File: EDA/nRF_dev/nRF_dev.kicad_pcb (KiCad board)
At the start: 2 copper layers, 52 x 82.7 mm, 60 parts, among them J1 USB_B_Micro, J2 Conn_01x02, J3 Conn_02x18_Odd_Even, J4 Conn_02x18_Odd_Even, J5 OV7675_DBG, J6 FH26W-25S-0.3SHW(60), J7 SWD, U1 NCP1117-3.3_SOT223, U2 W25Q128JVS, U3 RP2040, U4 OV7675pcb, Y1 ABLS-12.000MHZ-B4-T

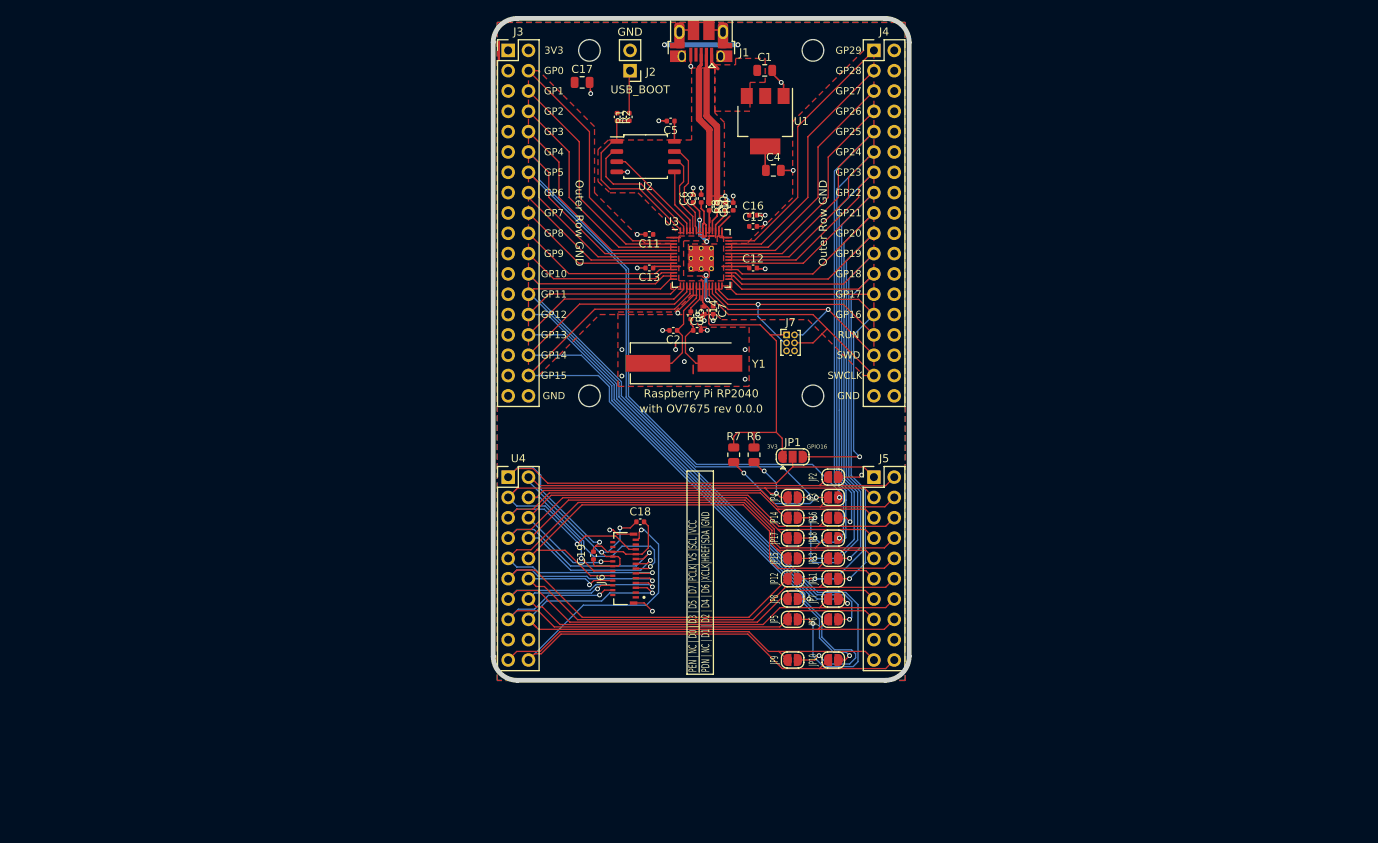
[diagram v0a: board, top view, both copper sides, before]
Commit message: adding layout work for nrf_dev pcb
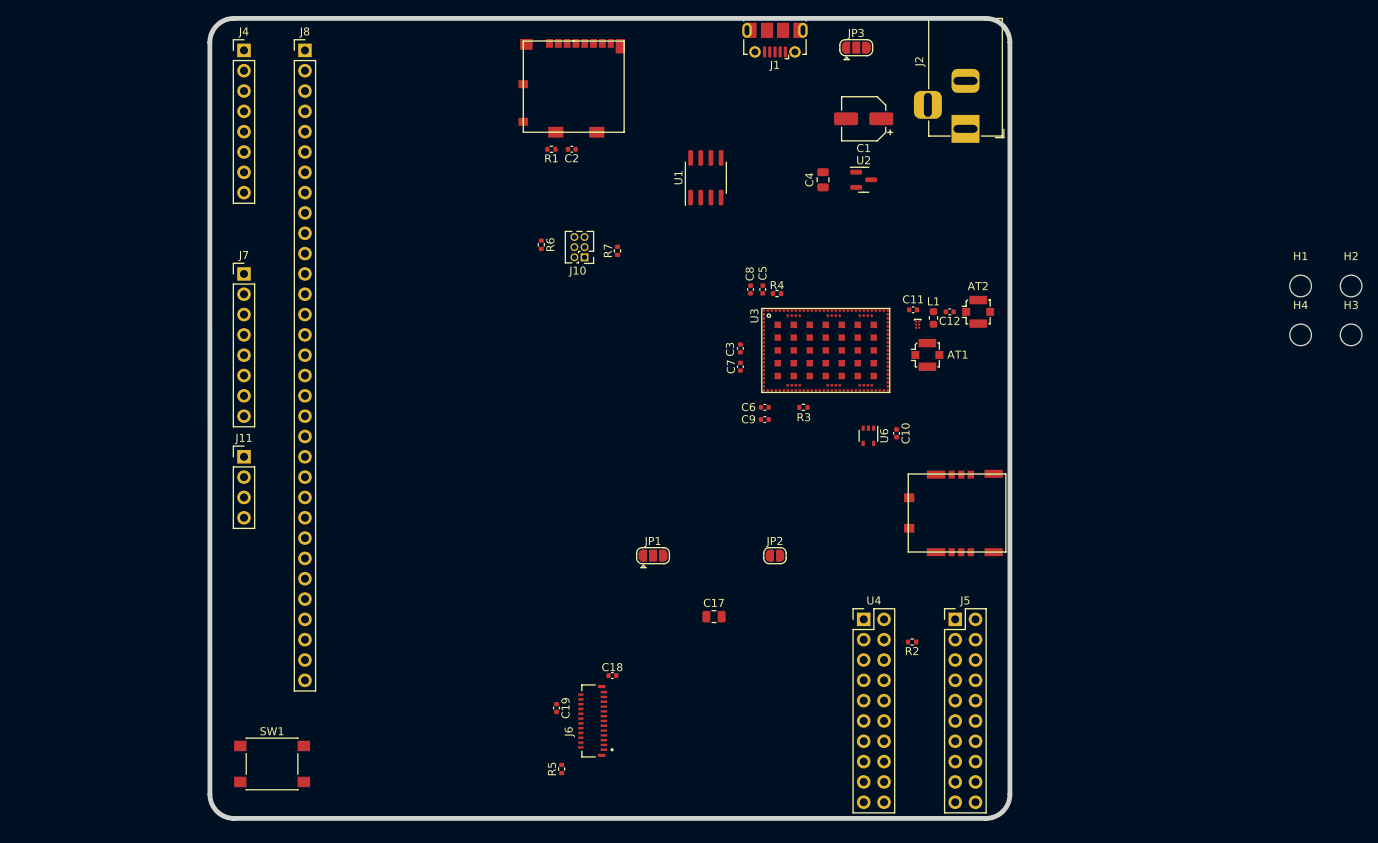
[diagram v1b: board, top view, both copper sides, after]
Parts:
- removed C13, C14, C15, C16: 100n, Capacitor_SMD:C_0402_1005Metric
- removed JP10, JP11, JP12, JP13, JP14, JP15, JP16, JP17, JP18, JP4, JP5, JP6, JP7, JP8, JP9: ., Jumper:SolderJumper-2_P1.3mm_Open_RoundedPad1.0x1.5mm
- removed Y1: ABLS-12.000MHZ-B4-T, RP2040_minimal:Crystal_SMD_HC49-US
- added AT1: AT-MAIN, Connector_Coaxial:U.FL_Molex_MCRF_73412-0110_Vertical, F.Cu at (128.3, 112.1)
- added AT2: AT-GNSS, Connector_Coaxial:U.FL_Molex_MCRF_73412-0110_Vertical, F.Cu at (134.6, 106.7)
- added J10: nRF_DBG, Connector_PinHeader_1.27mm:PinHeader_2x03_P1.27mm_Vertical, F.Cu at (85.4, 99.9)
- added J11: UART, Connector_PinHeader_2.54mm:PinHeader_1x04_P2.54mm_Vertical, F.Cu at (42.9, 124.8)
- added J8: Conn_01x32_Male, Connector_PinHeader_2.54mm:PinHeader_1x32_P2.54mm_Vertical, F.Cu at (50.5, 74.0)
- added J9: SIM, project:SIMNano, F.Cu at (138.1, 131.8)
- added L1: 9.1 nH, Inductor_SMD:L_0603_1608Metric, F.Cu at (129.0, 107.4)
- added SW1: RST, Button_Switch_SMD:SW_Push_1P1T_NO_6x6mm_H9.5mm, F.Cu at (46.4, 163.2)
- added U5: BGA524N6, project:TSNP-6-2, F.Cu at (126.9, 107.9)
- added U6: MSQA6V1W5T2G, Package_TO_SOT_SMD:SOT-353_SC-70-5, F.Cu at (120.9, 122.2)
- C1: value 10u -> 100 uF; footprint Capacitor_SMD:C_0805_2012Metric -> Capacitor_SMD:CP_Elec_5x5.8
- C10: value 1u -> 220 pF
- C11, C18, C19, C5: value 100n -> 100 nF
- C12: value 100n -> 1 nF
- C17, C4: value 10u -> 10 uF
- C2, C3: value 27p -> 100 nF
- C6, C9: value 100n -> 15 pF
- C7: value 100n -> 1 μF
- C8: value 1u -> 100 nF
- J1: footprint RP2040_minimal:USB_Micro-B_Amphenol_10103594-0001LF_Horizontal_modified -> Connector_USB:USB_Micro-B_Molex-105017-0001
- J2: value Conn_01x02 -> Jack-DC; footprint Connector_PinHeader_2.54mm:PinHeader_1x02_P2.54mm_Vertical -> Connector_BarrelJack:BarrelJack_Horizontal
- J3: value Conn_02x18_Odd_Even -> Micro_SD_Card; footprint Connector_PinHeader_2.54mm:PinHeader_2x18_P2.54mm_Vertical -> project:microSD_Connector
- J4: value Conn_02x18_Odd_Even -> Conn_01x08_Male; footprint Connector_PinHeader_2.54mm:PinHeader_2x18_P2.54mm_Vertical -> Connector_PinHeader_2.54mm:PinHeader_1x08_P2.54mm_Vertical
- J7: value SWD -> Conn_01x08_Male; footprint Connector_PinHeader_1.00mm:PinHeader_2x03_P1.00mm_Vertical -> Connector_PinHeader_2.54mm:PinHeader_1x08_P2.54mm_Vertical
- JP3: footprint Jumper:SolderJumper-2_P1.3mm_Open_RoundedPad1.0x1.5mm -> Jumper:SolderJumper-3_P1.3mm_Open_RoundedPad1.0x1.5mm
- R1: value 1k -> 100 kΩ; footprint Capacitor_SMD:C_0402_1005Metric -> Resistor_SMD:R_0402_1005Metric
- R2: value DNF -> 10 kΩ; footprint Capacitor_SMD:C_0402_1005Metric -> Resistor_SMD:R_0402_1005Metric
- R3, R4: value 27 -> 10 kΩ; footprint Capacitor_SMD:C_0402_1005Metric -> Resistor_SMD:R_0402_1005Metric
- R5: value 1k -> 10 kΩ; footprint Capacitor_SMD:C_0402_1005Metric -> Resistor_SMD:R_0402_1005Metric
- R6: value 4.7 kΩ -> 1 kΩ; footprint Resistor_SMD:R_0805_2012Metric -> Resistor_SMD:R_0402_1005Metric
- R7: value 4.7 kΩ -> 39 Ω; footprint Resistor_SMD:R_0805_2012Metric -> Resistor_SMD:R_0402_1005Metric
- U1: value NCP1117-3.3_SOT223 -> 23LCV1024-I/SN; footprint Package_TO_SOT_SMD:SOT-223-3_TabPin2 -> Package_SO:SOIC-8_3.9x4.9mm_P1.27mm
- U2: value W25Q128JVS -> MCP1700-3302E_SOT23; footprint Package_SO:SOIC-8_5.23x5.23mm_P1.27mm -> Package_TO_SOT_SMD:SOT-23
- U3: value RP2040 -> NRF9160; footprint RP2040_minimal:RP2040-QFN-56 -> project:nRF9160
- moved H1 93.7 mm to (174.9, 103.5)
- moved H4 89.2 mm to (174.9, 109.6)
- moved J4 78.7 mm to (42.9, 74.0)
- moved R2 75.3 mm to (126.4, 148.0), turned to 180 degrees
- moved H2 73.4 mm to (181.2, 103.5)
- moved C17 68.8 mm to (101.6, 144.8)
- moved J7 68.2 mm to (42.9, 101.9)
- moved H3 67.7 mm to (181.2, 109.6)
- moved R5 59.0 mm to (82.5, 163.8), turned to 90 degrees
- moved JP3 56.3 mm to (119.4, 73.7), turned to 0 degrees
- moved U4 47.9 mm to (120.3, 145.1)
- moved J2 42.6 mm to (133.0, 83.8), turned to -90 degrees
- moved R6 37.4 mm to (80.0, 98.3)
- moved C10 34.9 mm to (124.4, 121.9), turned to -90 degrees
- moved C11 34.3 mm to (126.5, 106.4)
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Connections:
- C1 pad 1: VBUS -> VPP
- C1 pad 2: GND -> -BATT
- C10 pad 1: +3V3 -> -BATT
- C10 pad 2: GND -> Net-(C10-Pad2)
- C11 pad 1: +3V3 -> -BATT
- C11 pad 2: GND -> V_3.3
- C12 pad 1: +3V3 -> Net-(AT2-Pad1)
- C12 pad 2: GND -> Net-(C12-Pad2)
- C17 pad 1: +3V3 -> V_3.3
- C17 pad 2: GND -> -BATT
- C2 pad 1: Net-(C2-Pad1) -> V_3.3
- C2 pad 2: GND -> -BATT
- C3 pad 1: Net-(C3-Pad1) -> V_3.3
- C3 pad 2: GND -> -BATT
- C4 pad 1: +3V3 -> V_3.3
- C4 pad 2: GND -> -BATT
- C5 pad 1: +3V3 -> VPP
- C5 pad 2: GND -> -BATT
- C6 pad 1: +1V1 -> VPP
- C6 pad 2: GND -> -BATT
- C7 pad 1: +1V1 -> -BATT
- C7 pad 2: GND -> Net-(C7-Pad2)
- C8 pad 1: +1V1 -> VPP
- C8 pad 2: GND -> -BATT
- C9 pad 1: +3V3 -> -BATT
- C9 pad 2: GND -> VPP
- J1 pad 1: VBUS -> V_USB
- J1 pad 2: /USB_D- -> unconnected-(J1-Pad2)
- J1 pad 3: /USB_D+ -> unconnected-(J1-Pad3)
- J1 pad 5: GND -> -BATT
- J1 pad 6: GND -> -BATT
- J2 pad 1: /~{USB_BOOT} -> +BATT
- J2 pad 2: GND -> -BATT
- J3 pad 1: GND -> unconnected-(J3-Pad1)
- J3 pad 2: +3V3 -> SD_CS
- J3 pad 3: GND -> SD_MOSI
- J3 pad 4: /GPIO0 -> V_3.3
- J3 pad 5: GND -> SD_SCLK
- J3 pad 6: /GPIO1 -> -BATT
- J3 pad 7: GND -> SD_MISO
- J3 pad 8: /GPIO2 -> unconnected-(J3-Pad8)
- J3 pad 9: GND -> -BATT
- J4 pad 1: /GPIO29_ADC3 -> -BATT
- J4 pad 2: GND -> VPP
- J4 pad 3: /GPIO28_ADC2 -> -BATT
- J4 pad 4: GND -> VPP
- J4 pad 5: /GPIO27_ADC1 -> -BATT
- J4 pad 6: GND -> V_3.3
- J4 pad 7: /GPIO26_ADC0 -> -BATT
- J4 pad 8: GND -> V_3.3
- J6 pad S1: GND -> -BATT
- J6 pad S2: GND -> -BATT
- J7 pad 1: +3V3 -> -BATT
- J7 pad 2: SWDIO -> V_3.3
- J7 pad 3: RST -> -BATT
- J7 pad 4: SWCLK -> V_3.3
- J7 pad 5: GND -> -BATT
- J7 pad 6: unconnected-(J7-Pad6) -> V_3.3
- JP1 pad 1: +3V3 -> V_3.3
- JP2 pad 1: GND -> -BATT
- JP3 pad 1: /GPIO4 -> V_USB
- JP3 pad 2: SDA -> VPP
- R1 pad 1: /QSPI_SS -> V_3.3
- R1 pad 2: /~{USB_BOOT} -> SD_CS
- R2 pad 1: +3V3 -> V_3.3
- R2 pad 2: /QSPI_SS -> SDA
- R3 pad 1: /USB_D+ -> V_3.3
- R3 pad 2: Net-(R3-Pad2) -> nRF_RST
- R4 pad 1: /USB_D- -> V_3.3
- R4 pad 2: Net-(R4-Pad2) -> nRF_EN
- R5 pad 1: Net-(R5-Pad1) -> V_3.3
- R5 pad 2: Net-(C3-Pad1) -> SCL
- R6 pad 1: +3V3 -> V_3.3
- R6 pad 2: SCL -> nRF_SWCLK
- R7 pad 1: +3V3 -> nRF_RST
- R7 pad 2: SDA -> Net-(J10-Pad3)
- U1 pad 1: GND -> FLASH_CS
- U1 pad 2: +3V3 -> FLASH_MISO
- U1 pad 3: VBUS -> unconnected-(U1-Pad3)
- U2 pad 1: /QSPI_SS -> -BATT
- U2 pad 2: /QSPI_SD1 -> V_3.3
- U2 pad 3: /QSPI_SD2 -> VPP
- U3 pad 1: +3V3 -> -BATT
- U3 pad 10: +3V3 -> unconnected-(U3-Pad10)
- U3 pad 11: /GPIO8 -> -BATT
- U3 pad 12: /GPIO9 -> V_3.3
- U3 pad 13: /GPIO10 -> Net-(C7-Pad2)
- U3 pad 14: /GPIO11 -> -BATT
- U3 pad 15: /GPIO12 -> CB_VIN
- U3 pad 16: /GPIO13 -> SCL
- U3 pad 17: /GPIO14 -> -BATT
- U3 pad 18: /GPIO15 -> SDA
- U3 pad 19: GND -> VS
- U3 pad 2: /GPIO0 -> CB_D5
- U3 pad 20: Net-(C2-Pad1) -> HREF
- U3 pad 21: Net-(R5-Pad1) -> -BATT
- U3 pad 22: +3V3 -> VPP
- U3 pad 23: +1V1 -> PCLK
- U3 pad 24: SWCLK -> XCLK
- U3 pad 25: SWDIO -> PEN
- U3 pad 26: RST -> PDN
- U3 pad 27: CB_VIN -> -BATT
- U3 pad 28: /GPIO17 -> Net-(J8-Pad18)
- U3 pad 29: /GPIO18 -> Net-(J8-Pad19)
- U3 pad 3: /GPIO1 -> CB_D6
- U3 pad 30: /GPIO19 -> Net-(J8-Pad20)
- U3 pad 31: /GPIO20 -> -BATT
- U3 pad 32: /GPIO21 -> nRF_RST
- U3 pad 33: +3V3 -> nRF_SWCLK
- U3 pad 34: /GPIO22 -> nRF_SWDIO
- U3 pad 35: /GPIO23 -> TX
- U3 pad 36: /GPIO24 -> -BATT
- U3 pad 37: /GPIO25 -> RX
- U3 pad 38: /GPIO26_ADC0 -> SD_SCLK
- U3 pad 39: /GPIO27_ADC1 -> SD_MISO
- U3 pad 4: /GPIO2 -> CB_D7
- U3 pad 40: /GPIO28_ADC2 -> SD_MOSI
- U3 pad 41: /GPIO29_ADC3 -> -BATT
- U3 pad 42: +3V3 -> SD_CS
- U3 pad 43: +3V3 -> Net-(U3-Pad43)
- U3 pad 44: +3V3 -> -BATT
- U3 pad 45: +1V1 -> unconnected-(U3-Pad45)
- U3 pad 46: Net-(R4-Pad2) -> Net-(U3-Pad46)
- U3 pad 47: Net-(R3-Pad2) -> -BATT
- U3 pad 48: +3V3 -> Net-(U3-Pad48)
- U3 pad 49: +3V3 -> Net-(C10-Pad2)
- U3 pad 5: /GPIO3 -> -BATT
- U3 pad 50: +1V1 -> -BATT
- U3 pad 51: /QSPI_SD3 -> unconnected-(U3-Pad51)
- U3 pad 52: /QSPI_SCLK -> -BATT
- U3 pad 53: /QSPI_SD0 -> unconnected-(U3-Pad53)
- U3 pad 54: /QSPI_SD2 -> unconnected-(U3-Pad54)
- U3 pad 55: /QSPI_SD1 -> unconnected-(U3-Pad55)
- U3 pad 56: /QSPI_SS -> -BATT
- U3 pad 57: GND -> unconnected-(U3-Pad57)
- U3 pad 6: /GPIO4 -> -BATT
- U3 pad 7: /GPIO5 -> -BATT
- U3 pad 8: /GPIO6 -> -BATT
- U3 pad 9: /GPIO7 -> -BATT
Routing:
- net /GPIO10: track 99.3 -> 0.00 mm, vias 1 -> 0
- net /GPIO4: track 93.1 -> 0.00 mm, vias 1 -> 0
- net /GPIO14: track 91.9 -> 0.00 mm, vias 1 -> 0
- net SDA: track 87.4 -> 0.00 mm, vias 3 -> 0
- net /GPIO5: track 86.5 -> 0.00 mm, vias 1 -> 0
- net /GPIO15: track 84.7 -> 0.00 mm, vias 1 -> 0
- net /GPIO24: track 82.1 -> 0.00 mm, vias 1 -> 0
- net PDN: track 81.2 -> 0.00 mm, vias 1 -> 0
- net /GPIO25: track 80.3 -> 0.00 mm, vias 1 -> 0
- net /GPIO11: track 80.0 -> 0.00 mm, vias 1 -> 0
- net /GPIO21: track 79.5 -> 0.00 mm, vias 1 -> 0
- net +3V3: track 78.9 -> 0.00 mm, vias 2 -> 0
- net CB_VCC: track 78.8 -> 0.00 mm, vias 1 -> 0
- net /GPIO12: track 77.8 -> 0.00 mm, vias 1 -> 0
- net CB_GND: track 75.7 -> 0.00 mm, vias 2 -> 0
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- removed copper zone on F.Cu, net +1V1
- removed copper zone on F.Cu, net +3V3
- removed copper zone on B.Cu, net GND
- removed copper zone on F.Cu, net GND
- removed copper zone on F.Cu, net VBUS
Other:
- board size 52 x 82.7 mm -> 100 x 100 mm
- board text removed: "3V3"
- board text removed: "GND"
- board text removed: "GP0"
- board text removed: "GP1"
- board text removed: "GP10"
- board text removed: "GP11"
- board text removed: "GP12"
- board text removed: "GP13"
- board text removed: "GP14"
- board text removed: "GP15"
- board text removed: "GP16"
- board text removed: "GP17"
- board text removed: "GP18"
- board text removed: "GP19"
- board text removed: "GP2"
- board text removed: "GP20"
- board text removed: "GP21"
- board text removed: "GP22"
- board text removed: "GP23"
- board text removed: "GP24"
- board text removed: "GP25"
- board text removed: "GP26"
- board text removed: "GP27"
- board text removed: "GP28"
- board text removed: "GP29"
- board text removed: "GP3"
- board text removed: "GP4"
- board text removed: "GP5"
- board text removed: "GP6"
- board text removed: "GP7"
- board text removed: "GP8"
- board text removed: "GP9"
- board text removed: "GPIO16"
- board text removed: "Outer Row GND"
- board text removed: "PEN | NC | D0 | D3 | D5 | D7 |PCLK| VS |SCL |VCC PDN | NC | D1 | D2 | D4 | D6 |XCLK|HREF|SDA |GND"
- board text removed: "RUN"
- board text removed: "Raspberry Pi RP2040"
- board text removed: "SWCLK"
- board text removed: "SWD"
- board text removed: "USB_BOOT"
- board text removed: "with OV7675 rev 0.0.0"

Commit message: more layout work
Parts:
- added SW2: BTA, Button_Switch_SMD:SW_Push_1P1T_NO_6x6mm_H9.5mm, F.Cu at (76.2, 76.2)
- J8: value Conn_01x32_Male -> Conn_01x15_Male; footprint Connector_PinHeader_2.54mm:PinHeader_1x32_P2.54mm_Vertical -> Connector_PinHeader_2.54mm:PinHeader_1x15_P2.54mm_Vertical
- moved H3 165.6 mm to (15.7, 111.7)
- moved H2 163.5 mm to (17.7, 103.2)
- moved H4 149.2 mm to (25.8, 112.1)
- moved H1 147.8 mm to (27.1, 101.9)
- moved SW1 95.2 mm to (111.8, 94.0), turned to -90 degrees
- moved J4 60.6 mm to (43.2, 134.6), turned to 180 degrees
- moved J11 51.1 mm to (43.2, 73.7)
- moved R2 42.1 mm to (84.3, 150.1), turned to -90 degrees
- moved R3 39.5 mm to (75.1, 130.6), turned to 90 degrees
- moved JP2 36.6 mm to (88.1, 167.1), turned to 180 degrees
- moved J8 35.3 mm to (48.3, 109.2), turned to 180 degrees
- moved R6 35.1 mm to (64.1, 129.6), turned to 90 degrees
- moved J10 34.4 mm to (69.5, 130.3)
- moved R7 34.4 mm to (73.7, 129.5)
- moved U4 31.0 mm to (99.1, 167.6), turned to 180 degrees
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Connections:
- C17 pad 1: V_3.3 -> CB_VCC
- C17 pad 2: -BATT -> CB_GND
- J8 pad 1: CB_D0 -> Net-(U3-Pad28)
- J8 pad 10: SCL -> FLASH_SCLK
- J8 pad 11: SDA -> FLASH_MOSI
- J8 pad 12: VS -> FLASH_CS
- J8 pad 13: HREF -> FLASH_MISO
- J8 pad 14: PCLK -> RX
- J8 pad 15: XCLK -> TX
- J8 pad 2: CB_D1 -> Net-(U3-Pad29)
- J8 pad 3: CB_D2 -> Net-(U3-Pad30)
- J8 pad 4: CB_D3 -> Net-(U3-Pad35)
- J8 pad 5: CB_D4 -> BTA
- J8 pad 6: CB_D5 -> SD_SCLK
- J8 pad 7: CB_D6 -> SD_MISO
- J8 pad 8: CB_D7 -> SD_MOSI
- J8 pad 9: CB_VIN -> SD_CS
- R2 pad 1: V_3.3 -> CB_VCC
- R5 pad 1: V_3.3 -> CB_VCC
- U3 pad 28: Net-(J8-Pad18) -> Net-(U3-Pad28)
- U3 pad 29: Net-(J8-Pad19) -> Net-(U3-Pad29)
- U3 pad 30: Net-(J8-Pad20) -> Net-(U3-Pad30)
- U3 pad 35: TX -> Net-(U3-Pad35)
- U3 pad 37: RX -> BTA
- U3 pad 84: FLASH_MISO -> FLASH_MOSI
- U3 pad 86: FLASH_MOSI -> FLASH_CS
- U3 pad 87: FLASH_CS -> FLASH_MISO
- U3 pad 88: nRF_PWR -> RX
- U3 pad 89: nRF_STAT -> TX
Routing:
- net VPP: track 0.00 -> 163.7 mm, vias 0 -> 3
- net nRF_RST: track 0.00 -> 160.0 mm, vias 0 -> 2
- net BTA: track 0.00 -> 158.1 mm, vias 0 -> 1
- net CB_D7: track 0.00 -> 140.8 mm, vias 0 -> 2
- net SD_MISO: track 0.00 -> 133.1 mm, vias 0 -> 3
- net CB_D5: track 0.00 -> 132.1 mm, vias 0 -> 2
- net SCL: track 0.00 -> 127.4 mm, vias 0 -> 2
- net SD_CS: track 0.00 -> 118.0 mm, vias 0 -> 2
- net SD_SCLK: track 0.00 -> 115.5 mm, vias 0 -> 2
- net CB_D3: track 0.00 -> 115.1 mm, vias 0 -> 2
- net SD_MOSI: track 0.00 -> 111.1 mm, vias 0 -> 2
- net CB_D1: track 0.00 -> 108.1 mm, vias 0 -> 2
- net VS: track 0.00 -> 108.0 mm, vias 0 -> 2
- net SDA: track 0.00 -> 106.4 mm, vias 0 -> 1
- net CB_D2: track 0.00 -> 105.4 mm, vias 0 -> 1
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- added copper zone on B.Cu, net -BATT
- added copper zone on B.Cu, net CB_GND
- added copper zone on F.Cu, net CB_VCC
- added copper zone on F.Cu, net V_3.3
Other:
- board size 100 x 100 mm -> 78.2 x 100 mm

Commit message: finished layout and gerber files for nRF dev camera
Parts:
- moved H3 88.7 mm to (103.0, 96.0)
- moved H4 56.6 mm to (43.0, 166.0)
- moved H2 50.8 mm to (68.0, 96.0)
- moved H1 44.1 mm to (43.0, 143.0)
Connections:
- J6 pad S1: -BATT -> CB_GND
- J6 pad S2: -BATT -> CB_GND
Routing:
- net -BATT: track 33.9 -> 309.3 mm, vias 13 -> 34
- net nRF_RST: track 160.0 -> 241.9 mm
- net V_3.3: track 22.3 -> 45.5 mm, vias 1 -> 6
- net CB_VCC: track 37.8 -> 57.5 mm
- net Net-(U3-Pad93): track 0.00 -> 17.9 mm, vias 0 -> 2
- net VPP: track 163.7 -> 175.6 mm
- net CB_GND: track 40.5 -> 45.2 mm, vias 4 -> 5
- net CB_D6: track 95.2 -> 90.8 mm
- net SD_MISO: track 133.1 -> 135.3 mm
- net Net-(J8-Pad4): track 78.6 -> 76.9 mm
- net CB_VIN: track 68.8 -> 67.4 mm
- net FLASH_MISO: track 62.5 -> 63.7 mm
- net SD_MOSI: track 111.1 -> 112.2 mm
- net BTA: track 158.1 -> 159.2 mm
- net SD_CS: track 118.0 -> 119.0 mm
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- added copper zone on F.Cu, net -BATT
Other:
- board text added: "3V3"
- board text added: "3V3|CB VIN"
- board text added: "BC"
- board text added: "BTA"
- board text added: "BoSL Camera dev"
- board text added: "CB GND"
- board text added: "CLK"
- board text added: "CS"
- board text added: "D0"
- board text added: "D1"
- board text added: "D2"
- board text added: "D3"
- board text added: "D4"
- board text added: "D5"
- board text added: "D6"
- board text added: "D7"
- board text added: "EN"
- board text added: "FLASH"
- board text added: "GND"
- board text added: "GNSS"
- board text added: "HREF"
- board text added: "IO"
- board text added: "LTE"
- board text added: "MISO"
- board text added: "MOSI"
- board text added: "NC"
- board text added: "P17"
- board text added: "P18"
- board text added: "P19"
- board text added: "P20"
- board text added: "PCLK"
- board text added: "PDN"
- board text added: "PEN"
- board text added: "RST"
- board text added: "RX"
- board text added: "SCL"
- board text added: "SCLK"
- board text added: "SD"
- board text added: "SDA"
- board text added: "SWD"
- board text added: "TX"
- board text added: "USB|BAT"
- board text added: "VCC"
- board text added: "VPP"
- board text added: "VS"
- board text added: "XCLK"
- board text added: "micro SD"
- board text added: "nano SIM"
- board text added: "rev 0.0.1"

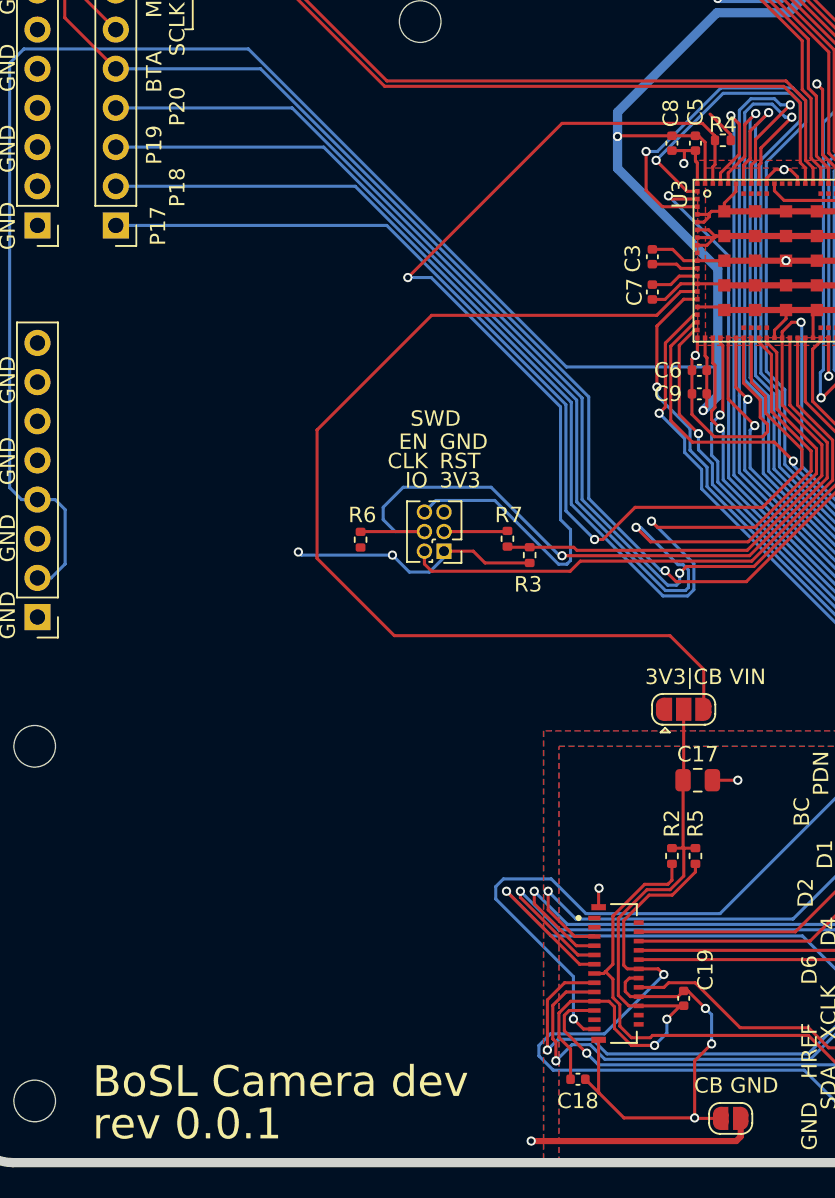
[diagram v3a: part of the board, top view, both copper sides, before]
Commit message: fixed pcb errors
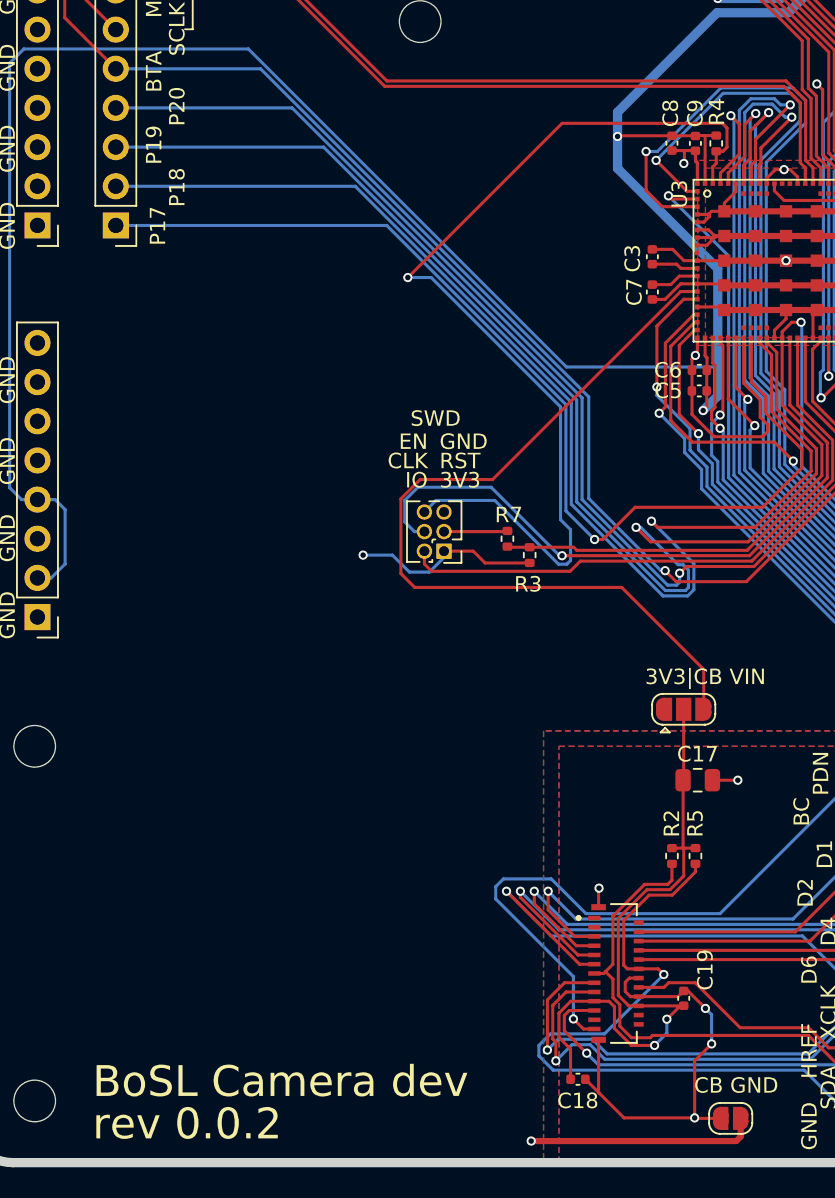
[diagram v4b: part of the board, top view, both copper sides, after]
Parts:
- removed R6: 1 kΩ, Resistor_SMD:R_0402_1005Metric
- moved C9 16.2 mm to (85.8, 103.9), turned to 90 degrees
- moved C5 16.1 mm to (86.1, 120.0), turned to 180 degrees
- moved R4 0.47 mm to (87.2, 103.9), turned to -90 degrees
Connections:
- R4 pad 1: V_3.3 -> VPP
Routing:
- net CB_VIN: track 67.4 -> 54.4 mm
- net nRF_SWCLK: track 51.3 -> 44.7 mm
- net V_3.3: track 45.5 -> 38.9 mm, vias 6 -> 5
- net nRF_EN: track 62.8 -> 64.4 mm
- net VPP: track 175.6 -> 176.8 mm
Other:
- board text added: "rev 0.0.2"
- board text removed: "rev 0.0.1"
